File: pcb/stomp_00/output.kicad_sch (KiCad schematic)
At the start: 2 parts, among them J15 Euro_Out_1, U3 TL072

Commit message: adding all the components...
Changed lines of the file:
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@@
 (kicad_sch (version 20230121) (generator eeschema)
   (paper "A4")
+  (text_box "Output stage, from line down to instrument level."
+    (at 107.95 22.86 0) (size 53.34 20.32)
+    (stroke (width 0) (type default))
+    (fill (type none))
+    (effects (font (size 1.27 1.27)) (justify left top))
+  )
   (symbol (lib_id "Amplifier_Operational:TL072") (at 74.295 62.23 0) (unit 2)
     (in_bom yes) (on_board yes) (dnp no) (fields_autoplaced)

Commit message: taking shape...
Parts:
- U3: footprint (none) -> Package_SO:SOIC-8_3.9x4.9mm_P1.27mm
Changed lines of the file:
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@@
       (effects (font (size 1.27 1.27)))
     )
-    (property "Footprint" "" (at 74.295 62.23 0)
+    (property "Footprint" "Package_SO:SOIC-8_3.9x4.9mm_P1.27mm" (at 74.295 62.23 0)
       (effects (font (size 1.27 1.27)) hide)
     )
@@
       (effects (font (size 1.27 1.27)))
     )
-    (property "Footprint" "" (at 73.66 45.72 0)
+    (property "Footprint" "Package_SO:SOIC-8_3.9x4.9mm_P1.27mm" (at 73.66 45.72 0)
       (effects (font (size 1.27 1.27)) hide)
     )
@@
       (effects (font (size 1.27 1.27)) (justify left))
     )
-    (property "Footprint" "" (at 76.2 81.915 0)
+    (property "Footprint" "Package_SO:SOIC-8_3.9x4.9mm_P1.27mm" (at 76.2 81.915 0)
       (effects (font (size 1.27 1.27)) hide)
     )

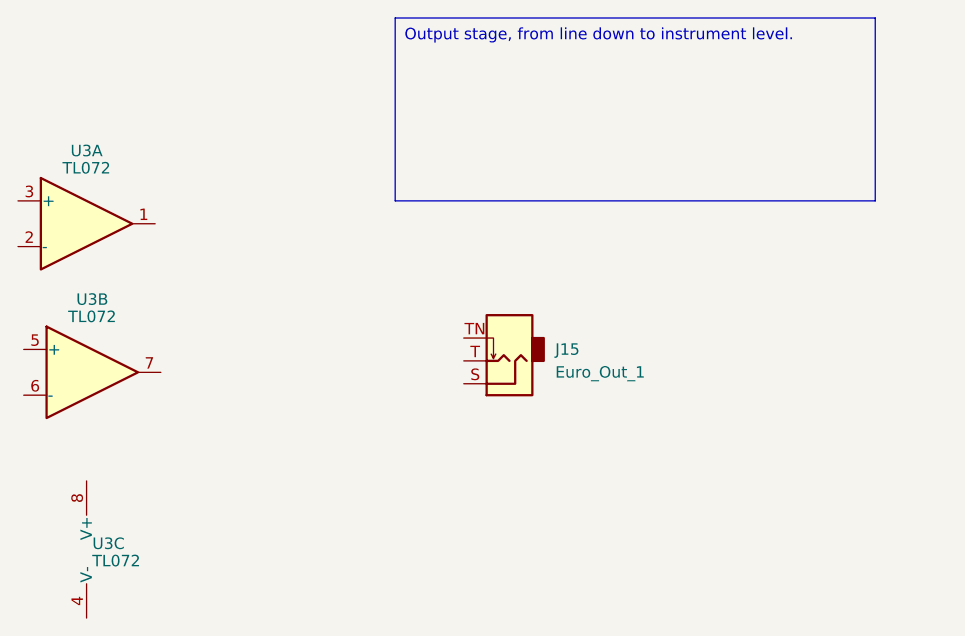
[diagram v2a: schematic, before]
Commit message: input stage schematic
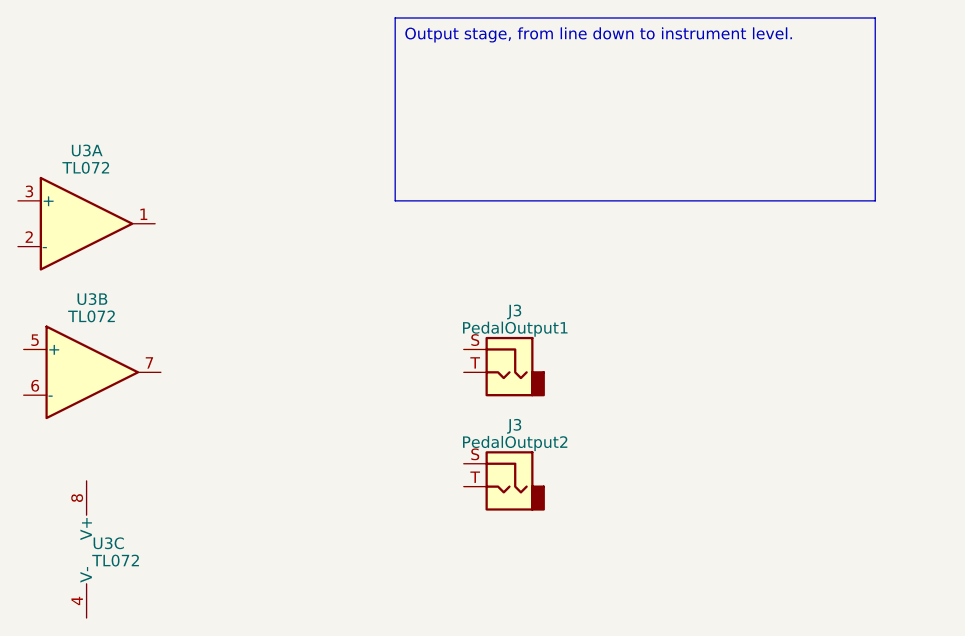
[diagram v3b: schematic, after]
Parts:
- removed J15: Euro_Out_1, AudioJacks:Jack_3.5mm_QingPu_WQP-PJ398SM_Vertical, symbol Connector_Audio:AudioJack2_SwitchT
- added J3: PedalOutput1, symbol Connector_Audio:AudioJack2
- added J3: PedalOutput2, symbol Connector_Audio:AudioJack2
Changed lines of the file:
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@@
     (effects (font (size 1.27 1.27)) (justify left top))
+  )
+  (symbol (lib_id "Connector_Audio:AudioJack2") (at 120.65 62.23 0) (mirror y) (unit 1)
+    (in_bom yes) (on_board yes) (dnp no) (fields_autoplaced)
+    (property "Reference" "J3" (at 121.285 55.4101 0)
+      (effects (font (size 1.27 1.27)))
+    )
+    (property "Value" "PedalOutput1" (at 121.285 57.3311 0)
+      (effects (font (size 1.27 1.27)))
+    )
+    (property "Footprint" "" (at 120.65 62.23 0)
+      (effects (font (size 1.27 1.27)) hide)
+    )
+    (property "Datasheet" "~" (at 120.65 62.23 0)
+      (effects (font (size 1.27 1.27)) hide)
+    )
+    (pin "S")
+    (pin "T")
+    (instances
+      (project "stomp_00"
+        (path "/8f4a2eb0-078b-46cb-b534-a4acd11d130e/9942492d-ba8b-45b2-b427-7fe14bedb7e0"
+          (reference "J3") (unit 1)
+        )
+        (path "/8f4a2eb0-078b-46cb-b534-a4acd11d130e/fb960d61-0706-49d5-ba88-99500a8c94ab"
+          (reference "J2") (unit 1)
+        )
+      )
+    )
   )
   (symbol (lib_id "Amplifier_Operational:TL072") (at 74.295 62.23 0) (unit 2)
@@
     )
   )
-  (symbol (lib_id "Connector_Audio:AudioJack2_SwitchT") (at 120.65 60.96 180) (unit 1)
+  (symbol (lib_id "Connector_Audio:AudioJack2") (at 120.65 74.93 0) (mirror y) (unit 1)
     (in_bom yes) (on_board yes) (dnp no) (fields_autoplaced)
-    (property "Reference" "J15" (at 125.73 59.69 0)
-      (effects (font (size 1.27 1.27)) (justify right))
+    (property "Reference" "J3" (at 121.285 68.1101 0)
+      (effects (font (size 1.27 1.27)))
     )
-    (property "Value" "Euro_Out_1" (at 125.73 62.23 0)
-      (effects (font (size 1.27 1.27)) (justify right))
+    (property "Value" "PedalOutput2" (at 121.285 70.0311 0)
+      (effects (font (size 1.27 1.27)))
     )
-    (property "Footprint" "AudioJacks:Jack_3.5mm_QingPu_WQP-PJ398SM_Vertical" (at 120.65 60.96 0)
+    (property "Footprint" "" (at 120.65 74.93 0)
       (effects (font (size 1.27 1.27)) hide)
     )
-    (property "Datasheet" "~" (at 120.65 60.96 0)
+    (property "Datasheet" "~" (at 120.65 74.93 0)
       (effects (font (size 1.27 1.27)) hide)
     )
     (pin "S")
     (pin "T")
-    (pin "TN")
     (instances
-      (project "dk2_01"
-        (path "/87a59a99-d509-467e-85da-26d34072acb7/a1783777-3c7d-4cc4-9255-28fca529e5f7"
-          (reference "J15") (unit 1)
+      (project "stomp_00"
+        (path "/8f4a2eb0-078b-46cb-b534-a4acd11d130e/9942492d-ba8b-45b2-b427-7fe14bedb7e0"
+          (reference "J3") (unit 1)
         )
-        (path "/87a59a99-d509-467e-85da-26d34072acb7/be1ddc4d-f499-4b75-b4b5-b626a320d90d"
-          (reference "J23") (unit 1)
-        )
-        (path "/87a59a99-d509-467e-85da-26d34072acb7/a3b4dd4a-c522-40f2-b825-f444d434bc45"
-          (reference "J6") (unit 1)
+        (path "/8f4a2eb0-078b-46cb-b534-a4acd11d130e/fb960d61-0706-49d5-ba88-99500a8c94ab"
+          (reference "J8") (unit 1)
         )
       )
-      (project "stomp_00"
-        (path "/8f4a2eb0-078b-46cb-b534-a4acd11d130e"
-          (reference "J2") (unit 1)
-        )
-        (path "/8f4a2eb0-078b-46cb-b534-a4acd11d130e/fb960d61-0706-49d5-ba88-99500a8c94ab"
-          (reference "J2") (unit 1)
-        )
-      )
